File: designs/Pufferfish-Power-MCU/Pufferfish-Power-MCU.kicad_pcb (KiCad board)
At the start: 2 copper layers, 157.7 x 102.6 mm, 282 parts, among them J1 172316-1108, J2 PB_TO_STM32, J3 Molex_MicroFit_2P, J4 1722871202, J5 1722871202, J6 1722871202, Q1 SiR158DP, Q12 2N7002E, Q13 2N7002E, Q2 SiR158DP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

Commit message: Fixed footprints
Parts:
- moved U7 44.9 mm to (145.1, 52.9)
- moved U10 42.1 mm to (68.0, 82.4)
- moved Q6 36.8 mm to (64.2, 70.6)
- moved U8 33.9 mm to (58.5, 105.9)
- moved Q5 29.5 mm to (61.0, 91.9)
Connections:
- C10 pad 1: Net-(C10-Pad1) -> (no net)
- C10 pad 2: Net-(C10-Pad2) -> (no net)
- C11 pad 1: Net-(C11-Pad1) -> (no net)
- C3 pad 1: Net-(C3-Pad1) -> (no net)
- C8 pad 2: /LTC4015/LTC4421-CPO -> (no net)
- C91 pad 1: Net-(C91-Pad1) -> (no net)
- JP10 pad 2: /LTC7812/OV_2_2 -> (no net)
- JP7 pad 1: /LTC7812/PGOOD2 -> (no net)
- L3 pad 1: Net-(L3-Pad1) -> (no net)
- L3 pad 2: Net-(L3-Pad2) -> (no net)
- R14 pad 1: LTC4421-PWR-nCH1 -> (no net)
- R14 pad 2: Net-(R14-Pad2) -> (no net)
- R15 pad 1: LTC4421-PWR-nVALID1 -> (no net)
- R15 pad 2: Net-(R15-Pad2) -> (no net)
- R16 pad 1: LTC4421-PWR-nFAULT1 -> (no net)
- R16 pad 2: Net-(R16-Pad2) -> (no net)
- R17 pad 1: LTC4421-PWR-nCH2 -> (no net)
- R17 pad 2: Net-(R17-Pad2) -> (no net)
- R18 pad 1: LTC4421-PWR-nVALID2 -> (no net)
- R18 pad 2: Net-(R18-Pad2) -> (no net)
- R19 pad 1: LTC4421-PWR-nFAULT2 -> (no net)
- R19 pad 2: Net-(R19-Pad2) -> (no net)
- R20 pad 2: LTC4421-PWR-nDISABLE1 -> (no net)
- R21 pad 2: LTC4421-PWR-nDISABLE2 -> (no net)
- R23 pad 1: Net-(R23-Pad1) -> (no net)
- R6 pad 1: Net-(R6-Pad1) -> (no net)
- R8 pad 1: Net-(R8-Pad1) -> (no net)
- U1 pad 11: Net-(U1-Pad11) -> (no net)
- U1 pad 12: Net-(U1-Pad12) -> (no net)
- U1 pad 15: Net-(U1-Pad15) -> (no net)
- U1 pad 18: Net-(U1-Pad18) -> (no net)
- U1 pad 19: Net-(U1-Pad19) -> (no net)
- U1 pad 20: Net-(U1-Pad20) -> (no net)
- U1 pad 22: Net-(U1-Pad22) -> (no net)
- U1 pad 23: Net-(U1-Pad23) -> (no net)
- U1 pad 24: Net-(U1-Pad24) -> (no net)
- U1 pad 25: Net-(U1-Pad25) -> (no net)
- U1 pad 26: Net-(U1-Pad26) -> (no net)
- U1 pad 29: Net-(U1-Pad29) -> (no net)
- U1 pad 30: Net-(U1-Pad30) -> (no net)
- U1 pad 31: Net-(U1-Pad31) -> (no net)
- U1 pad 32: Net-(U1-Pad32) -> (no net)
- U1 pad 33: Net-(U1-Pad33) -> (no net)
- U1 pad 34: Net-(U1-Pad34) -> (no net)
- U1 pad 35: Net-(U1-Pad35) -> (no net)
- U1 pad 8: Net-(U1-Pad8) -> (no net)
- U5 pad 23: Net-(U5-Pad23) -> (no net)
- U5 pad 5: Net-(U5-Pad5) -> (no net)
- U6 pad 6: Net-(U6-Pad6) -> (no net)
- U6 pad 9: Net-(U6-Pad9) -> (no net)

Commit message: Fixed 7812 symbol bug
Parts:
- added U11: LTC7812-LTC7812, Package_DFN_QFN:QFN-32-1EP_5x5mm_P0.5mm_EP3.45x3.45mm, F.Cu at (224.5, 71.5)
- moved Q5 157.7 mm to (215.6, 123.4)
- moved Q6 157.7 mm to (218.7, 102.1)
- moved U10 157.7 mm to (222.6, 113.9)
- moved U8 157.7 mm to (213.0, 137.4)
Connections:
- C91 pad 1: (no net) -> Net-(C91-Pad1)
- JP10 pad 2: (no net) -> /LTC7812/OV_2_2
- JP7 pad 1: (no net) -> /LTC7812/PGOOD2
- U10 pad 4: (no net) -> /LTC7812/TG_2_2
- U5 pad 5: (no net) -> /LTC7812/ITH_1_1
- U9 pad 4: (no net) -> /LTC7812/BG_2_2

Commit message: Board setup, 3.3V regulator placement
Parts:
- added F1: Fuse, Fuse:Fuseholder_Cylinder-6.3x32mm_Schurter_0031-8002_Horizontal_Open, F.Cu at (106.7, 53.3)
- moved U8 211.0 mm to (127.6, -55.5)
- moved L3 176.0 mm to (186.4, -42.8)
- moved H1 161.4 mm to (155.7, -2.16)
- moved R50 161.0 mm to (235.3, 34.8)
- moved R53 156.5 mm to (42.0, -0.60)
- moved C1 148.4 mm to (85.8, 29.2)
- moved C10 148.4 mm to (99.1, 19.3)
- moved C11 148.4 mm to (102.0, 19.3)
- moved C14 148.4 mm to (13.5, 14.1)
- moved C15 148.4 mm to (75.2, 34.2)
- moved C16 148.4 mm to (90.7, 19.3)
- moved C2 148.4 mm to (82.9, 34.7)
- moved C25 148.4 mm to (97.7, 4.53)
- moved C27 148.4 mm to (52.0, -40.4)
- moved C28 148.4 mm to (52.0, -38.5)
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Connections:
- C10 pad 1: (no net) -> Net-(C10-Pad1)
- C10 pad 2: (no net) -> Net-(C10-Pad2)
- C11 pad 1: (no net) -> Net-(C11-Pad1)
- C3 pad 1: (no net) -> Net-(C3-Pad1)
- C8 pad 2: (no net) -> /LTC4015/LTC4421-CPO
- L3 pad 1: (no net) -> Net-(L3-Pad1)
- L3 pad 2: (no net) -> Net-(L3-Pad2)
- R14 pad 1: (no net) -> LTC4421-PWR-nCH1
- R14 pad 2: (no net) -> Net-(R14-Pad2)
- R15 pad 1: (no net) -> LTC4421-PWR-nVALID1
- R15 pad 2: (no net) -> Net-(R15-Pad2)
- R16 pad 1: (no net) -> LTC4421-PWR-nFAULT1
- R16 pad 2: (no net) -> Net-(R16-Pad2)
- R17 pad 1: (no net) -> LTC4421-PWR-nCH2
- R17 pad 2: (no net) -> Net-(R17-Pad2)
- R18 pad 1: (no net) -> LTC4421-PWR-nVALID2
- R18 pad 2: (no net) -> Net-(R18-Pad2)
- R19 pad 1: (no net) -> LTC4421-PWR-nFAULT2
- R19 pad 2: (no net) -> Net-(R19-Pad2)
- R20 pad 2: (no net) -> LTC4421-PWR-nDISABLE1
- R21 pad 2: (no net) -> LTC4421-PWR-nDISABLE2
- R23 pad 1: (no net) -> Net-(R23-Pad1)
- R6 pad 1: (no net) -> Net-(R6-Pad1)
- R8 pad 1: (no net) -> Net-(R8-Pad1)
- U1 pad 11: (no net) -> Net-(U1-Pad11)
- U1 pad 12: (no net) -> Net-(U1-Pad12)
- U1 pad 15: (no net) -> Net-(U1-Pad15)
- U1 pad 18: (no net) -> Net-(U1-Pad18)
- U1 pad 19: (no net) -> Net-(U1-Pad19)
- U1 pad 20: (no net) -> Net-(U1-Pad20)
- U1 pad 22: (no net) -> Net-(U1-Pad22)
- U1 pad 23: (no net) -> Net-(U1-Pad23)
- U1 pad 24: (no net) -> Net-(U1-Pad24)
- U1 pad 25: (no net) -> Net-(U1-Pad25)
- U1 pad 26: (no net) -> Net-(U1-Pad26)
- U1 pad 29: (no net) -> Net-(U1-Pad29)
- U1 pad 30: (no net) -> Net-(U1-Pad30)
- U1 pad 31: (no net) -> Net-(U1-Pad31)
- U1 pad 32: (no net) -> Net-(U1-Pad32)
- U1 pad 33: (no net) -> Net-(U1-Pad33)
- U1 pad 34: (no net) -> Net-(U1-Pad34)
- U1 pad 35: (no net) -> Net-(U1-Pad35)
- U1 pad 8: (no net) -> Net-(U1-Pad8)
- U11 pad 1: (no net) -> Net-(U11-Pad1)
- U11 pad 2: (no net) -> Net-(U11-Pad2)
- U11 pad 23: (no net) -> Net-(U11-Pad23)
- U11 pad 31: (no net) -> Net-(U11-Pad31)
- U11 pad 32: (no net) -> Net-(U11-Pad32)
- U11 pad 4: (no net) -> Net-(U11-Pad4)
- U11 pad 5: (no net) -> Net-(U11-Pad5)
- U11 pad 6: (no net) -> Net-(U11-Pad6)
- U11 pad 7: (no net) -> Net-(U11-Pad7)
- U11 pad 8: (no net) -> Net-(U11-Pad8)
- U5 pad 23: (no net) -> Net-(U5-Pad23)
- U6 pad 6: (no net) -> Net-(U6-Pad6)
- U6 pad 9: (no net) -> Net-(U6-Pad9)
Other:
- board size 157.7 x 102.6 mm -> 121.9 x 71.1 mm
- copper layers 2 -> 4
- board text added: "3V3 PGOOD"

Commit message: Placement
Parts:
- moved C33 1.28 mm to (161.6, 76.3), turned to 90 degrees
- moved R32 1.27 mm to (163.3, 75.7)
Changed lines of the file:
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@@
     (38 B.Mask user)
     (39 F.Mask user)
-    (40 Dwgs.User user)
+    (40 Dwgs.User user hide)
     (41 Cmts.User user)
     (42 Eco1.User user)
@@
     (pad_to_mask_clearance 0)
     (aux_axis_origin 0 0)
-    (visible_elements 7FFFFF7F)
+    (visible_elements 7FFDF777)
     (pcbplotparams
       (layerselection 0x010fc_ffffffff)
@@
   )
   (module Pufferfish:CAP_SMD_0805 (layer F.Cu)
-    (at 160.9575 77.4 180)
+    (at 161.6456 76.3247 90)
     (descr "Capacitor SMD 0805 (2012 Metric), square (rectangular) end terminal, IPC_7351 nominal, (Body size source: https://docs.google.com/spreadsheets/d/1BsfQQcO9C6DZCsRaXUlFlo91Tg2WpOkGARC1WS5S8t0/edit?usp=sharing), generated with kicad-footprint-generator")
     (tags capacitor)
     (attr smd)
-    (fp_text reference C33 (at 3.1727 -0.2732) (layer F.SilkS)
+    (fp_text reference C33 (at 3.1727 -0.2732 90) (layer F.SilkS)
       (effects (font (size 1 1) (thickness 0.15)))
     )
-    (fp_text value CAP_22uF_25V_X5R_0805 (at 0 1.65) (layer F.Fab)
+    (fp_text value CAP_22uF_25V_X5R_0805 (at 0 1.65 90) (layer F.Fab)
       (effects (font (size 1 1) (thickness 0.15)))
     )
@@
     (fp_line (start 1.68 -0.95) (end 1.68 0.95) (layer F.CrtYd) (width 0.05))
     (fp_line (start 1.68 0.95) (end -1.68 0.95) (layer F.CrtYd) (width 0.05))
-    (fp_text user %R (at 0 0) (layer F.Fab)
+    (fp_text user %R (at 0.1801 0 90) (layer F.Fab)
       (effects (font (size 0.5 0.5) (thickness 0.08)))
     )
-    (pad 1 smd roundrect (at -0.9375 0 180) (size 0.975 1.4) (layers F.Cu F.Paste F.Mask) (roundrect_rratio 0.25)
+    (pad 1 smd roundrect (at -0.9375 0 90) (size 0.975 1.4) (layers F.Cu F.Paste F.Mask) (roundrect_rratio 0.25)
       (net 10 VIN_7812_2))
-    (pad 2 smd roundrect (at 0.9375 0 180) (size 0.975 1.4) (layers F.Cu F.Paste F.Mask) (roundrect_rratio 0.25)
+    (pad 2 smd roundrect (at 0.9375 0 90) (size 0.975 1.4) (layers F.Cu F.Paste F.Mask) (roundrect_rratio 0.25)
       (net 2 GND))
     (model ${KISYS3DMOD}/Capacitor_SMD.3dshapes/C_0805_2012Metric.wrl
@@
   )
   (module Pufferfish:RES_SMD_0402 (layer F.Cu)
-    (at 163.35 76.9898 90)
+    (at 163.35 75.715 90)
     (descr "Resistor SMD 0402 (1005 Metric), square (rectangular) end terminal, IPC_7351 nominal, (Body size source: http://www.tortai-tech.com/upload/download/2011102023233369053.pdf), generated with kicad-footprint-generator")
     (tags resistor)
@@
       (effects (font (size 1 1) (thickness 0.15)))
     )
-    (fp_text user %R (at 0 0 90) (layer F.Fab)
+    (fp_text user %R (at 0.0278 0.0736 90) (layer F.Fab)
       (effects (font (size 0.25 0.25) (thickness 0.04)))
     )

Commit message: Placement changes
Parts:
- moved L1 159.9 mm to (170.7, 85.5)
- moved C45 157.3 mm to (175.0, 69.1)
- moved C56 155.8 mm to (170.6, 89.9), turned to 180 degrees
- moved C43 154.9 mm to (179.8, 82.9), turned to 90 degrees
- moved C42 150.2 mm to (176.3, 82.9), turned to 90 degrees
- moved D5 142.3 mm to (159.8, 70.9)
- moved R35 141.8 mm to (172.8, 78.6), turned to 180 degrees
- moved R33 141.4 mm to (172.8, 80.4), turned to 180 degrees
- moved C39 140.1 mm to (172.7, 77.1)
- moved C44 138.6 mm to (166.8, 69.0), turned to 180 degrees
- moved R30 138.4 mm to (166.3, 75.7), turned to 180 degrees
- moved R31 135.8 mm to (166.7, 73.7)
- moved C35 134.6 mm to (162.0, 76.8), turned to 180 degrees
- moved C38 133.8 mm to (169.4, 76.7)
- moved R57 133.8 mm to (138.2, 96.5)
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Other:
- board text added: "5V PGOOD"

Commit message: Placements updated
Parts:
- C66, C70, JP1, JP2, JP3, JP4, JP5, JP6, R47, R48, R51, R74: moved to B.Cu
- moved C27 158.7 mm to (168.7, 67.1)
- moved C28 153.2 mm to (163.0, 67.1), turned to 180 degrees
- moved C29 150.9 mm to (160.8, 67.1)
- moved C30 145.7 mm to (155.4, 67.1), turned to 180 degrees
- moved R78 142.3 mm to (109.2, 94.6), turned to 180 degrees
- moved TP17 140.1 mm to (149.1, 101.3)
- moved R51 138.4 mm to (86.8, 93.0), turned to 180 degrees
- moved R_SENSE_1 136.6 mm to (93.4, 94.6), turned to 270 degrees
- moved TP15 136.5 mm to (149.1, 107.7)
- moved R77 135.7 mm to (91.4, 87.0)
- moved R_SENSE_2 135.1 mm to (101.6, 98.4), turned to 180 degrees
- moved R80 134.2 mm to (107.3, 99.1), turned to 90 degrees
- moved U8 132.0 mm to (101.3, 73.9)
- moved C75 129.5 mm to (98.4, 95.2), turned to 270 degrees
- moved U9 129.1 mm to (120.9, 83.3)
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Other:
- board text added: "Configuration Jumpers"
- board text added: "INT"
- board text added: "KILL"
- board text added: "Optional Pull-Ups"
- board text added: "PGOOD"
- board text added: "RUN"
- board text added: "Track Optional"

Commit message: Updated placement
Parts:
- added ?: , , F.Cu at (172.7, 195.7)
- added ?: , , F.Cu at (85.5, 103.4)
- added ?: , , F.Cu at (85.2, 99.1)
- added ?: , , F.Cu at (86.6, 96.3)
- added ?: , , F.Cu at (84.6, 99.2)
- C89, C90: value CAP_SMD_0603 -> CAP_SMD_0402; footprint Pufferfish:CAP_SMD_0603 -> Pufferfish:CAP_SMD_0402
- C91: value CAP_SMD_0603 -> 0.1u; footprint Pufferfish:CAP_SMD_0603 -> Pufferfish:CAP_SMD_0402
- C98: value CAP_SMD_0603 -> 1200pF
- C99, JP11, JP12, JP13, JP14, JP15, Q12, R53, TP20: moved to B.Cu
- J4, J5, J6: value 1722871202 -> Molex_UltraFit_1722871202
- L2: value LOGO_PUFFERFISH -> LOGO
- R11: footprint Pufferfish:RES_SMD_1206 -> Pufferfish:RES_SMD_0603
- R42, R57, R58: footprint Pufferfish:RES_SMD_1206 -> Pufferfish:RES_SMD_0603; moved to B.Cu
- R47, R48, R49, R50, R51, R52, R73, R74, R75, R76, R77, R78, R79, R80, R81, R_SENSE_1, R_SENSE_2, R_SENSE_3: value RES_SMD_1206 -> RES_SMD_0603; footprint Pufferfish:RES_SMD_1206 -> Pufferfish:RES_SMD_0603
- R72: value RES_SMD_1206 -> 35.7k; footprint Pufferfish:RES_SMD_1206 -> Pufferfish:RES_SMD_0603
- R90, R91, R92, R95, R97: value RES_SMD_1206 -> RES_SMD_0603; footprint Pufferfish:RES_SMD_1206 -> Pufferfish:RES_SMD_0603; moved to B.Cu
- R93: value RES_SMD_1206 -> 549k; footprint Pufferfish:RES_SMD_1206 -> Pufferfish:RES_SMD_0603
- R94: value RES_SMD_1206 -> 28.7k; footprint Pufferfish:RES_SMD_1206 -> Pufferfish:RES_SMD_0603
- R96: value RES_SMD_1206 -> 53.6k; footprint Pufferfish:RES_SMD_1206 -> Pufferfish:RES_SMD_0603
- moved R96 153.1 mm to (123.6, 81.5)
- moved C99 147.0 mm to (138.0, 70.2), turned to 270 degrees
- moved L6 145.3 mm to (131.6, 81.1)
- moved R97 143.3 mm to (135.4, 65.8)
- moved R_SENSE_3 143.0 mm to (124.7, 76.9), turned to 180 degrees
- moved R95 142.5 mm to (132.2, 72.9), turned to 90 degrees
- moved C93 140.3 mm to (127.2, 77.1), turned to 270 degrees
- moved JP8 139.2 mm to (108.3, 107.1)
- moved TP21 137.4 mm to (86.5, 96.2)
- moved C98 134.7 mm to (123.6, 79.4), turned to 180 degrees
- moved JP9 134.7 mm to (108.3, 109.9), turned to 180 degrees
- moved JP7 134.4 mm to (108.3, 104.2)
- moved TP3 133.6 mm to (85.5, 103.4)
- moved JP10 132.8 mm to (108.3, 112.6), turned to 180 degrees
- moved R94 132.4 mm to (119.4, 78.9), turned to 180 degrees
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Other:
- board text added: "EXTVCC2 Selection, DEF GND."
- board text added: "Optional, GND Default"
- board text added: "Power Board V2_0"

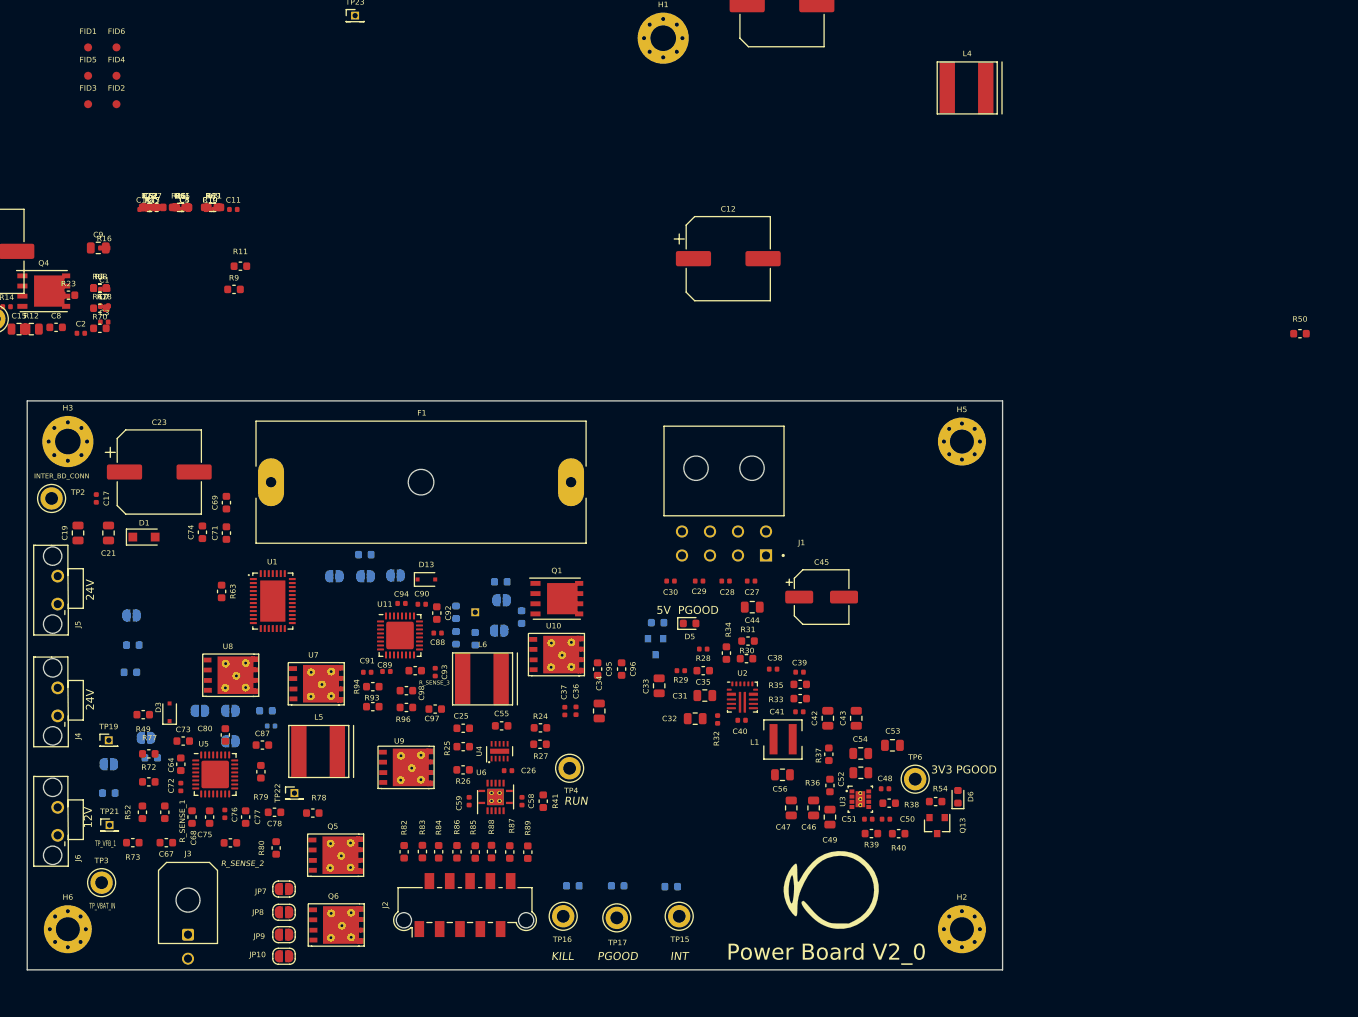
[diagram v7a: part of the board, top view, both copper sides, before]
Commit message: Revised placement as per feedback
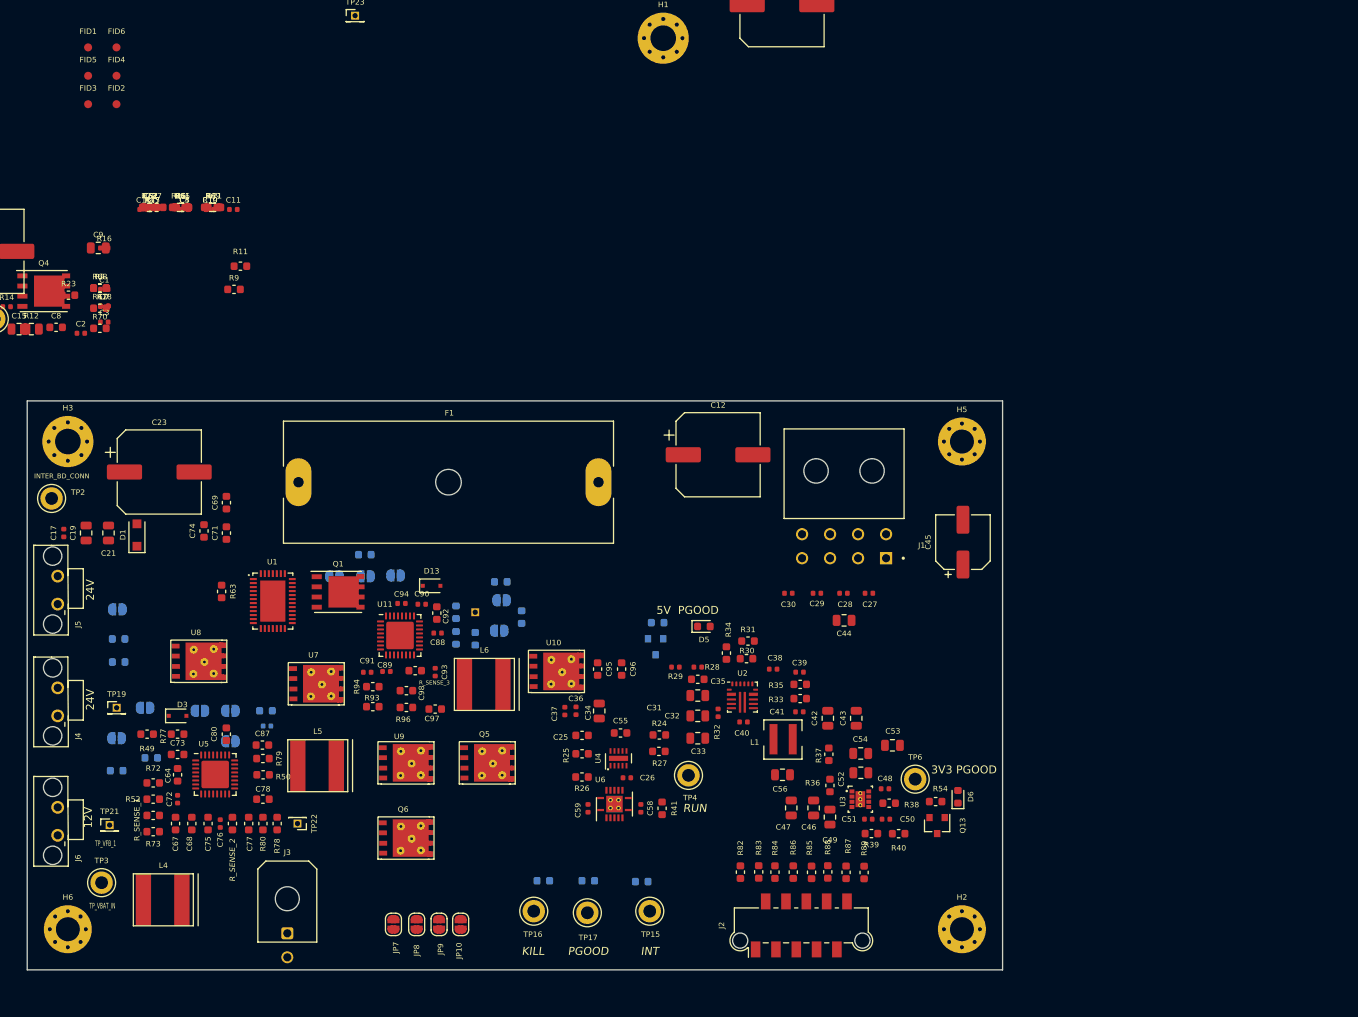
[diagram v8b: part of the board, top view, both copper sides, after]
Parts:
- L2: moved to B.Cu
- moved L4 142.8 mm to (91.7, 108.7)
- moved R50 140.8 mm to (105.7, 89.9)
- moved R82 42.1 mm to (165.4, 102.1)
- moved R83 42.1 mm to (167.6, 102.1)
- moved R84 42.1 mm to (169.7, 102.1)
- moved R85 42.1 mm to (174.2, 102.1)
- moved R86 42.1 mm to (172.0, 102.1)
- moved R87 42.1 mm to (178.6, 102.1)
- moved R88 42.1 mm to (176.3, 102.1)
- moved R89 42.1 mm to (180.8, 102.1)
- moved J2 42.1 mm to (173.0, 108.7)
- moved L2 29.6 mm to (173.7, 77.2), turned to 180 degrees
- moved Q1 27.4 mm to (115.1, 67.1)
- moved C12 24.5 mm to (162.6, 49.9)
- moved JP10 22.4 mm to (130.4, 108.6), turned to 270 degrees
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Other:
- board text added: "Pufferfish Power Board V2_0"
- board text added: "www.pez-globo.org"
- board text removed: "Power Board V2_0"
